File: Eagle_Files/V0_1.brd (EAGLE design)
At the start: 102.5 x 52.1 mm, 22 parts

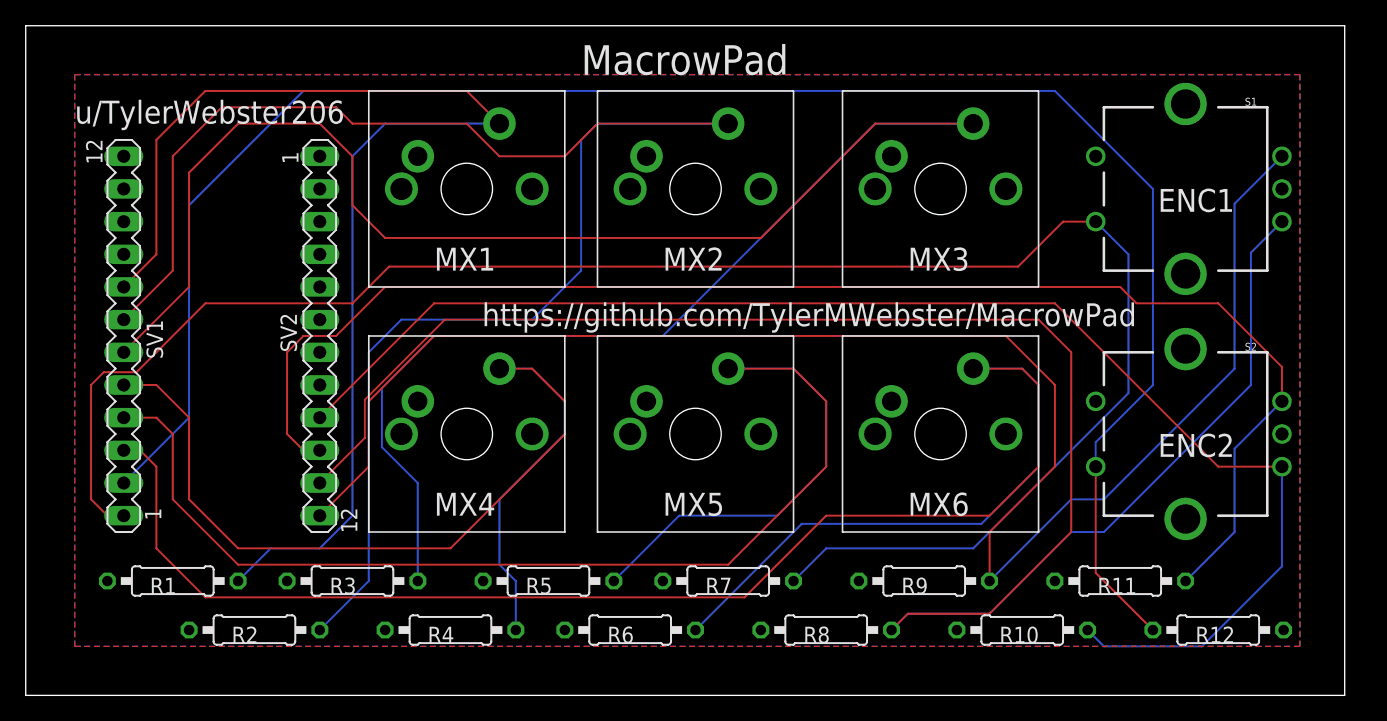
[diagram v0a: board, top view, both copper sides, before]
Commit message: Fixed switch spacing
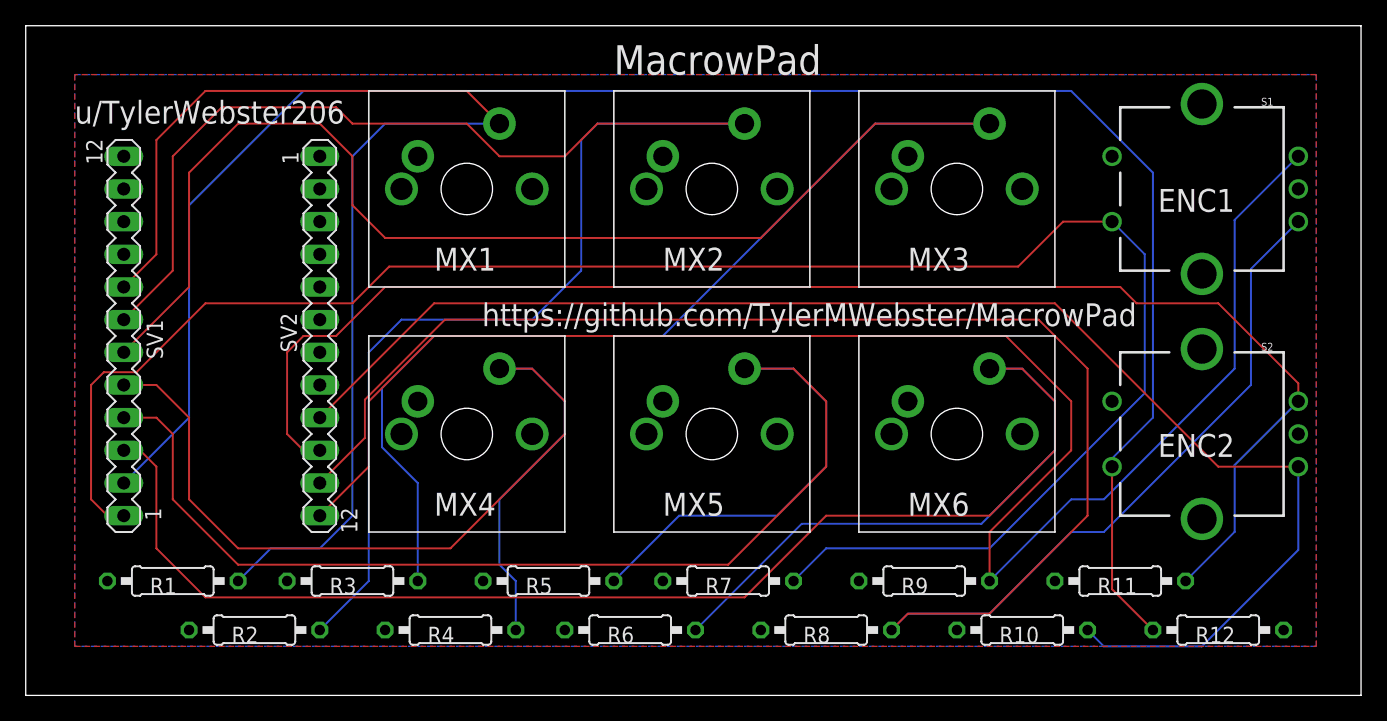
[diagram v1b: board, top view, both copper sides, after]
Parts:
- moved S1 1.27 mm to (88.9, 67.3)
- moved S2 1.27 mm to (88.9, 48.3)
- moved U$2 1.27 mm to (50.8, 67.3)
- moved U$3 1.27 mm to (69.8, 67.3)
- moved U$4 1.27 mm to (69.8, 48.3)
- moved U$5 1.27 mm to (50.8, 48.3)
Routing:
- net N$9: track 141.8 -> 144.3 mm
- net N$5: track 113.2 -> 110.6 mm
- net N$2: track 126.1 -> 128.6 mm
- net N$3: track 158.8 -> 161.4 mm
- net N$11: track 109.7 -> 111.5 mm
- net N$8: track 147.1 -> 148.7 mm
- net N$7: track 128.8 -> 130.3 mm
- net N$10: track 111.2 -> 112.2 mm
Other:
- board size 102.5 x 52.1 mm -> 103.8 x 52.1 mm
